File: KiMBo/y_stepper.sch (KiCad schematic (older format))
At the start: 25 parts, among them U25 TMC2130

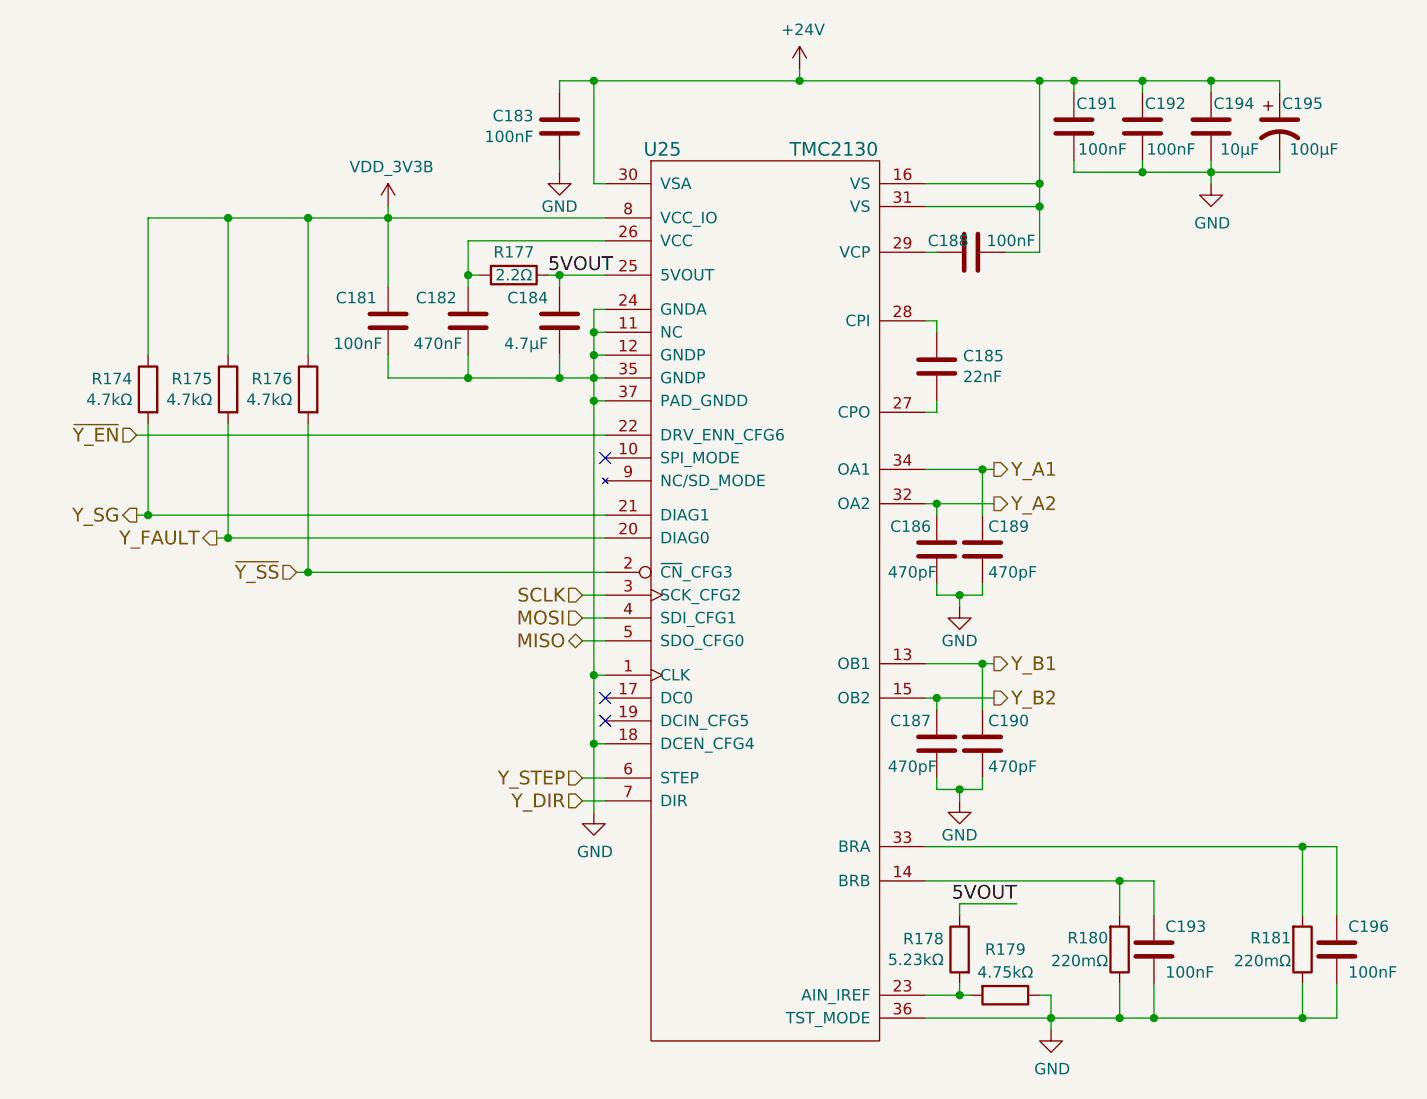
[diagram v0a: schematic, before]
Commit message: Leave SPI0 free for a display, reassign pins so SPI1 is available
Fix some typos/errors
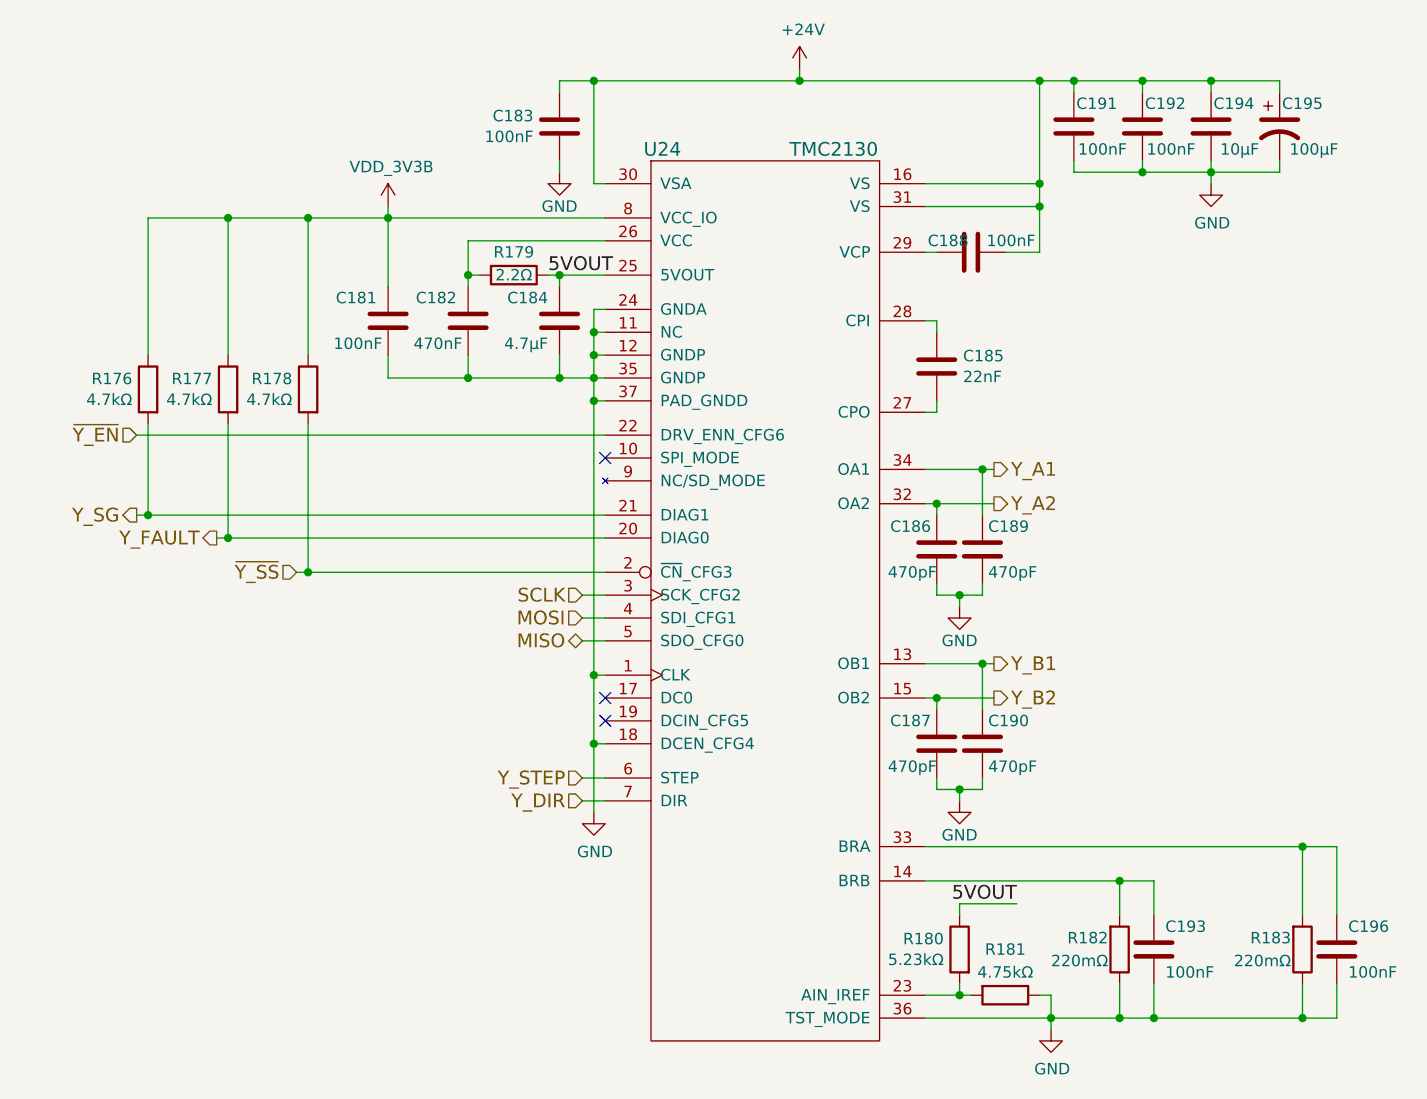
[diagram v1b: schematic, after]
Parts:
- renumbered R174 to R176, R175 to R177, R176 to R178, R177 to R179, R178 to R180, R179 to R181, R180 to R182, R181 to R183, U25 to U24
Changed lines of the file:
@@
 $EndComp
 $Comp
-L GND #PWR0248
+L GND #PWR0247
 U 1 1 58C0B231
 P 6550 3450
-F 0 "#PWR0248" H 6550 3200 50  0001 C CNN
+F 0 "#PWR0247" H 6550 3200 50  0001 C CNN
 F 1 "GND" H 6550 3300 50  0000 C CNN
 F 2 "" H 6550 3450 50  0000 C CNN
@@
 $EndComp
 $Comp
-L GND #PWR0249
+L GND #PWR0248
 U 1 1 58C0B23E
 P 9400 3500
-F 0 "#PWR0249" H 9400 3250 50  0001 C CNN
+F 0 "#PWR0248" H 9400 3250 50  0001 C CNN
 F 1 "GND" H 9405 3327 50  0000 C CNN
 F 2 "" H 9400 3500 50  0000 C CNN
@@
 $EndComp
 $Comp
-L +24V #PWR0250
+L +24V #PWR0249
 U 1 1 58C0B244
 P 7600 3000
-F 0 "#PWR0250" H 7600 2850 50  0001 C CNN
+F 0 "#PWR0249" H 7600 2850 50  0001 C CNN
 F 1 "+24V" H 7615 3173 50  0000 C CNN
 F 2 "" H 7600 3000 50  0000 C CNN
@@
 $EndComp
 $Comp
-L R R181
+L R R183
 U 1 1 58C0B251
 P 9800 6850
-F 0 "R181" H 9750 6800 50  0000 R CNN
+F 0 "R183" H 9750 6800 50  0000 R CNN
 F 1 "220mΩ" H 9750 6900 50  0000 R CNN
 F 2 "" V 9730 6850 50  0001 C CNN
@@
 $EndComp
 $Comp
-L R R180
+L R R182
 U 1 1 58C0B258
 P 9000 6850
-F 0 "R180" H 8950 6800 50  0000 R CNN
+F 0 "R182" H 8950 6800 50  0000 R CNN
 F 1 "220mΩ" H 8950 6900 50  0000 R CNN
 F 2 "" V 8930 6850 50  0001 C CNN
@@
 $EndComp
 $Comp
-L GND #PWR0251
+L GND #PWR0250
 U 1 1 58C0B25F
 P 8700 7200
-F 0 "#PWR0251" H 8700 6950 50  0001 C CNN
+F 0 "#PWR0250" H 8700 6950 50  0001 C CNN
 F 1 "GND" H 8705 7027 50  0000 C CNN
 F 2 "" H 8700 7200 50  0000 C CNN
@@
 NoConn ~ 6750 5750
 $Comp
-L R R177
+L R R179
 U 1 1 58C0B266
 P 6350 3900
-F 0 "R177" V 6250 3900 50  0000 C CNN
+F 0 "R179" V 6250 3900 50  0000 C CNN
 F 1 "2.2Ω" V 6350 3900 50  0000 C CNN
 F 2 "" V 6280 3900 50  0001 C CNN
@@
 NoConn ~ 6750 5850
 $Comp
-L GND #PWR0252
+L GND #PWR0251
 U 1 1 58C0B282
 P 6700 6250
-F 0 "#PWR0252" H 6700 6000 50  0001 C CNN
+F 0 "#PWR0251" H 6700 6000 50  0001 C CNN
 F 1 "GND" H 6705 6077 50  0000 C CNN
 F 2 "" H 6700 6250 50  0000 C CNN
@@
 Y_FAULT
 $Comp
-L R R175
+L R R177
 U 1 1 58C0B290
 P 5100 4400
-F 0 "R175" H 5169 4446 50  0000 L CNN
+F 0 "R177" H 5169 4446 50  0000 L CNN
 F 1 "4.7kΩ" H 5169 4355 50  0000 L CNN
 F 2 "" V 5030 4400 50  0001 C CNN
@@
 5VOUT
 $Comp
-L R R178
+L R R180
 U 1 1 58C0B2A2
 P 8300 6850
-F 0 "R178" H 8369 6896 50  0000 L CNN
+F 0 "R180" H 8369 6896 50  0000 L CNN
 F 1 "5.23kΩ" H 8369 6805 50  0000 L CNN
 F 2 "" V 8230 6850 50  0001 C CNN
@@
 5VOUT
 $Comp
-L R R179
+L R R181
 U 1 1 58C0B2AA
 P 8500 7050
-F 0 "R179" V 8300 7050 50  0000 C CNN
+F 0 "R181" V 8300 7050 50  0000 C CNN
 F 1 "4.75kΩ" V 8400 7050 50  0000 C CNN
 F 2 "" V 8430 7050 50  0001 C CNN
@@
 $EndComp
 $Comp
-L R R176
+L R R178
 U 1 1 58C0B2B1
 P 5450 4400
-F 0 "R176" H 5519 4446 50  0000 L CNN
+F 0 "R178" H 5519 4446 50  0000 L CNN
 F 1 "4.7kΩ" H 5519 4355 50  0000 L CNN
 F 2 "" V 5380 4400 50  0001 C CNN
@@
 $EndComp
 $Comp
-L GND #PWR0253
+L GND #PWR0252
 U 1 1 58C0B2C6
 P 8300 5350
-F 0 "#PWR0253" H 8300 5100 50  0001 C CNN
+F 0 "#PWR0252" H 8300 5100 50  0001 C CNN
 F 1 "GND" H 8300 5200 50  0000 C CNN
 F 2 "" H 8300 5350 50  0000 C CNN
@@
 $EndComp
 $Comp
-L GND #PWR0254
+L GND #PWR0253
 U 1 1 58C0B2DA
 P 8300 6200
-F 0 "#PWR0254" H 8300 5950 50  0001 C CNN
+F 0 "#PWR0253" H 8300 5950 50  0001 C CNN
 F 1 "GND" H 8300 6050 50  0000 C CNN
 F 2 "" H 8300 6200 50  0000 C CNN
@@
 $EndComp
 $Comp
-L TMC2130 U25
+L TMC2130 U24
 U 1 1 58C0B2E7
 P 7450 4850
-F 0 "U25" H 7000 6350 60  0000 C CNN
+F 0 "U24" H 7000 6350 60  0000 C CNN
 F 1 "TMC2130" H 7750 6350 60  0000 C CNN
 F 2 "" H 7450 5150 60  0001 C CNN
@@
 	8200 6150 8200 6100
 $Comp
-L R R174
+L R R176
 U 1 1 58C0B35B
 P 4750 4400
-F 0 "R174" H 4819 4446 50  0000 L CNN
+F 0 "R176" H 4819 4446 50  0000 L CNN
 F 1 "4.7kΩ" H 4819 4355 50  0000 L CNN
 F 2 "" V 4680 4400 50  0001 C CNN
@@
 	4750 3650 6750 3650
 $Comp
-L VDD_3V3B #PWR0255
+L VDD_3V3B #PWR0254
 U 1 1 5A300CA5
 P 5800 3600
-F 0 "#PWR0255" H 5800 3450 50  0001 C CNN
+F 0 "#PWR0254" H 5800 3450 50  0001 C CNN
 F 1 "VDD_3V3B" H 5815 3773 50  0000 C CNN
 F 2 "" H 5800 3600 50  0000 C CNN

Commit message: Use fixed 5V LM2592HV Buck, include SPI0 header for LCD
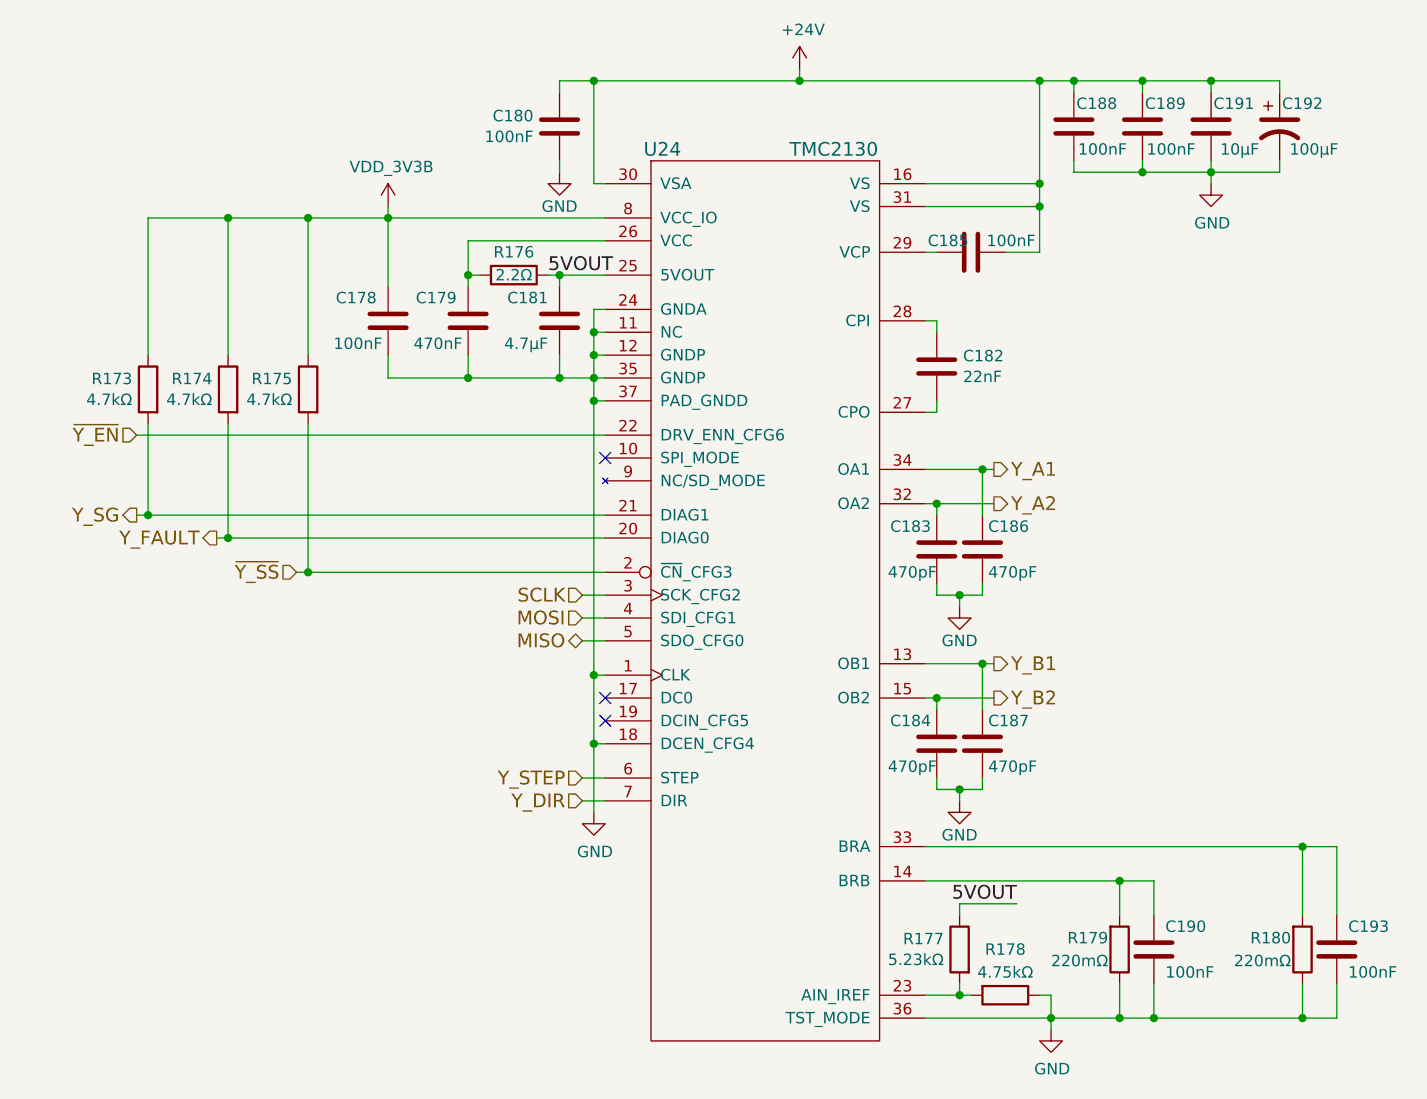
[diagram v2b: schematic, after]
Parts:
- renumbered C181 to C178, C182 to C179, C183 to C180, C184 to C181, C185 to C182, C186 to C183, C187 to C184, C188 to C185, C189 to C186, C190 to C187, C191 to C188, C192 to C189, C193 to C190, C194 to C191, C195 to C192, C196 to C193, R176 to R173, R177 to R174, R178 to R175, R179 to R176, R180 to R177, R181 to R178, R182 to R179, R183 to R180
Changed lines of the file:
@@
 Y_SG
 $Comp
-L C C183
+L C C180
 U 1 1 58C0B215
 P 6550 3250
-F 0 "C183" H 6436 3204 50  0000 R CNN
+F 0 "C180" H 6436 3204 50  0000 R CNN
 F 1 "100nF" H 6436 3295 50  0000 R CNN
 F 2 "Capacitors_SMD:C_0603" H 6588 3100 50  0001 C CNN
@@
 $EndComp
 $Comp
-L C C188
+L C C185
 U 1 1 58C0B21C
 P 8350 3800
-F 0 "C188" V 8300 3700 50  0000 C CNN
+F 0 "C185" V 8300 3700 50  0000 C CNN
 F 1 "100nF" V 8300 3975 50  0000 C CNN
 F 2 "Capacitors_SMD:C_0603" H 8388 3650 50  0001 C CNN
@@
 $EndComp
 $Comp
-L CP1 C195
+L CP1 C192
 U 1 1 58C0B223
 P 9700 3250
-F 0 "C195" H 9800 3350 50  0000 C CNN
+F 0 "C192" H 9800 3350 50  0000 C CNN
 F 1 "100μF" H 9850 3150 50  0000 C CNN
 F 2 "Capacitors_SMD:c_elec_8x10" H 9700 3250 50  0001 C CNN
@@
 $EndComp
 $Comp
-L C C191
+L C C188
 U 1 1 58C0B22A
 P 8800 3250
-F 0 "C191" H 8700 3350 50  0000 C CNN
+F 0 "C188" H 8700 3350 50  0000 C CNN
 F 1 "100nF" H 8675 3150 50  0000 C CNN
 F 2 "Capacitors_SMD:C_0603" H 8838 3100 50  0001 C CNN
@@
 $EndComp
 $Comp
-L GND #PWR0247
+L GND #PWR0242
 U 1 1 58C0B231
 P 6550 3450
-F 0 "#PWR0247" H 6550 3200 50  0001 C CNN
+F 0 "#PWR0242" H 6550 3200 50  0001 C CNN
 F 1 "GND" H 6550 3300 50  0000 C CNN
 F 2 "" H 6550 3450 50  0000 C CNN
@@
 $EndComp
 $Comp
-L C C192
+L C C189
 U 1 1 58C0B237
 P 9100 3250
-F 0 "C192" H 9000 3350 50  0000 C CNN
+F 0 "C189" H 9000 3350 50  0000 C CNN
 F 1 "100nF" H 8975 3150 50  0000 C CNN
 F 2 "Capacitors_SMD:C_0603" H 9138 3100 50  0001 C CNN
@@
 $EndComp
 $Comp
-L GND #PWR0248
+L GND #PWR0243
 U 1 1 58C0B23E
 P 9400 3500
-F 0 "#PWR0248" H 9400 3250 50  0001 C CNN
+F 0 "#PWR0243" H 9400 3250 50  0001 C CNN
 F 1 "GND" H 9405 3327 50  0000 C CNN
 F 2 "" H 9400 3500 50  0000 C CNN
@@
 $EndComp
 $Comp
-L +24V #PWR0249
+L +24V #PWR0244
 U 1 1 58C0B244
 P 7600 3000
-F 0 "#PWR0249" H 7600 2850 50  0001 C CNN
+F 0 "#PWR0244" H 7600 2850 50  0001 C CNN
 F 1 "+24V" H 7615 3173 50  0000 C CNN
 F 2 "" H 7600 3000 50  0000 C CNN
@@
 $EndComp
 $Comp
-L C C185
+L C C182
 U 1 1 58C0B24A
 P 8200 4300
-F 0 "C185" H 8315 4346 50  0000 L CNN
+F 0 "C182" H 8315 4346 50  0000 L CNN
 F 1 "22nF" H 8315 4255 50  0000 L CNN
 F 2 "Capacitors_SMD:C_0402" H 8238 4150 50  0001 C CNN
@@
 $EndComp
 $Comp
-L R R183
+L R R180
 U 1 1 58C0B251
 P 9800 6850
-F 0 "R183" H 9750 6800 50  0000 R CNN
+F 0 "R180" H 9750 6800 50  0000 R CNN
 F 1 "220mΩ" H 9750 6900 50  0000 R CNN
 F 2 "" V 9730 6850 50  0001 C CNN
@@
 $EndComp
 $Comp
-L R R182
+L R R179
 U 1 1 58C0B258
 P 9000 6850
-F 0 "R182" H 8950 6800 50  0000 R CNN
+F 0 "R179" H 8950 6800 50  0000 R CNN
 F 1 "220mΩ" H 8950 6900 50  0000 R CNN
 F 2 "" V 8930 6850 50  0001 C CNN
@@
 $EndComp
 $Comp
-L GND #PWR0250
+L GND #PWR0245
 U 1 1 58C0B25F
 P 8700 7200
-F 0 "#PWR0250" H 8700 6950 50  0001 C CNN
+F 0 "#PWR0245" H 8700 6950 50  0001 C CNN
 F 1 "GND" H 8705 7027 50  0000 C CNN
 F 2 "" H 8700 7200 50  0000 C CNN
@@
 NoConn ~ 6750 5750
 $Comp
-L R R179
+L R R176
 U 1 1 58C0B266
 P 6350 3900
-F 0 "R179" V 6250 3900 50  0000 C CNN
+F 0 "R176" V 6250 3900 50  0000 C CNN
 F 1 "2.2Ω" V 6350 3900 50  0000 C CNN
 F 2 "" V 6280 3900 50  0001 C CNN
@@
 $EndComp
 $Comp
-L C C182
+L C C179
 U 1 1 58C0B26D
 P 6150 4100
-F 0 "C182" H 6200 4200 50  0000 L CNN
+F 0 "C179" H 6200 4200 50  0000 L CNN
 F 1 "470nF" H 6175 4000 50  0000 L CNN
 F 2 "Capacitors_SMD:C_0603" H 6188 3950 50  0001 C CNN
@@
 NoConn ~ 6750 5850
 $Comp
-L GND #PWR0251
+L GND #PWR0246
 U 1 1 58C0B282
 P 6700 6250
-F 0 "#PWR0251" H 6700 6000 50  0001 C CNN
+F 0 "#PWR0246" H 6700 6000 50  0001 C CNN
 F 1 "GND" H 6705 6077 50  0000 C CNN
 F 2 "" H 6700 6250 50  0000 C CNN
@@
 $EndComp
 $Comp
-L C C193
+L C C190
 U 1 1 58C0B288
 P 9150 6850
-F 0 "C193" H 9200 6950 50  0000 L CNN
+F 0 "C190" H 9200 6950 50  0000 L CNN
 F 1 "100nF" H 9200 6750 50  0000 L CNN
 F 2 "Capacitors_SMD:C_0603" H 9188 6700 50  0001 C CNN
@@
 Y_FAULT
 $Comp
-L R R177
+L R R174
 U 1 1 58C0B290
 P 5100 4400
-F 0 "R177" H 5169 4446 50  0000 L CNN
+F 0 "R174" H 5169 4446 50  0000 L CNN
 F 1 "4.7kΩ" H 5169 4355 50  0000 L CNN
 F 2 "" V 5030 4400 50  0001 C CNN
@@
 NoConn ~ 6750 4700
 $Comp
-L C C184
+L C C181
 U 1 1 58C0B29A
 P 6550 4100
-F 0 "C184" H 6600 4200 50  0000 L CNN
+F 0 "C181" H 6600 4200 50  0000 L CNN
 F 1 "4.7μF" H 6600 4000 50  0000 L CNN
 F 2 "Capacitors_SMD:C_0402" H 6588 3950 50  0001 C CNN
@@
 5VOUT
 $Comp
-L R R180
+L R R177
 U 1 1 58C0B2A2
 P 8300 6850
-F 0 "R180" H 8369 6896 50  0000 L CNN
+F 0 "R177" H 8369 6896 50  0000 L CNN
 F 1 "5.23kΩ" H 8369 6805 50  0000 L CNN
 F 2 "" V 8230 6850 50  0001 C CNN
@@
 5VOUT
 $Comp
-L R R181
+L R R178
 U 1 1 58C0B2AA
 P 8500 7050
-F 0 "R181" V 8300 7050 50  0000 C CNN
+F 0 "R178" V 8300 7050 50  0000 C CNN
 F 1 "4.75kΩ" V 8400 7050 50  0000 C CNN
 F 2 "" V 8430 7050 50  0001 C CNN
@@
 $EndComp
 $Comp
-L R R178
+L R R175
 U 1 1 58C0B2B1
 P 5450 4400
-F 0 "R178" H 5519 4446 50  0000 L CNN
+F 0 "R175" H 5519 4446 50  0000 L CNN
 F 1 "4.7kΩ" H 5519 4355 50  0000 L CNN
 F 2 "" V 5380 4400 50  0001 C CNN
@@
 $EndComp
 $Comp
-L C C196
+L C C193
 U 1 1 58C0B2B8
 P 9950 6850
-F 0 "C196" H 10000 6950 50  0000 L CNN
+F 0 "C193" H 10000 6950 50  0000 L CNN
 F 1 "100nF" H 10000 6750 50  0000 L CNN
 F 2 "Capacitors_SMD:C_0603" H 9988 6700 50  0001 C CNN
@@
 $EndComp
 $Comp
-L C C186
+L C C183
 U 1 1 58C0B2BF
 P 8200 5100
-F 0 "C186" H 8225 5200 50  0000 L CNN
+F 0 "C183" H 8225 5200 50  0000 L CNN
 F 1 "470pF" H 8200 5000 50  0000 L CNN
 F 2 "Capacitors_SMD:C_0603" H 8238 4950 50  0001 C CNN
@@
 $EndComp
 $Comp
-L GND #PWR0252
+L GND #PWR0247
 U 1 1 58C0B2C6
 P 8300 5350
-F 0 "#PWR0252" H 8300 5100 50  0001 C CNN
+F 0 "#PWR0247" H 8300 5100 50  0001 C CNN
 F 1 "GND" H 8300 5200 50  0000 C CNN
 F 2 "" H 8300 5350 50  0000 C CNN
@@
 $EndComp
 $Comp
-L C C189
+L C C186
 U 1 1 58C0B2CC
 P 8400 5100
-F 0 "C189" H 8425 5200 50  0000 L CNN
+F 0 "C186" H 8425 5200 50  0000 L CNN
 F 1 "470pF" H 8425 5000 50  0000 L CNN
 F 2 "Capacitors_SMD:C_0603" H 8438 4950 50  0001 C CNN
@@
 $EndComp
 $Comp
-L C C187
+L C C184
 U 1 1 58C0B2D3
 P 8200 5950
-F 0 "C187" H 8225 6050 50  0000 L CNN
+F 0 "C184" H 8225 6050 50  0000 L CNN
 F 1 "470pF" H 8200 5850 50  0000 L CNN
 F 2 "Capacitors_SMD:C_0603" H 8238 5800 50  0001 C CNN
@@
 $EndComp
 $Comp
-L GND #PWR0253
+L GND #PWR0248
 U 1 1 58C0B2DA
 P 8300 6200
-F 0 "#PWR0253" H 8300 5950 50  0001 C CNN
+F 0 "#PWR0248" H 8300 5950 50  0001 C CNN
 F 1 "GND" H 8300 6050 50  0000 C CNN
 F 2 "" H 8300 6200 50  0000 C CNN
@@
 $EndComp
 $Comp
-L C C190
+L C C187
 U 1 1 58C0B2E0
 P 8400 5950
-F 0 "C190" H 8425 6050 50  0000 L CNN
+F 0 "C187" H 8425 6050 50  0000 L CNN
 F 1 "470pF" H 8425 5850 50  0000 L CNN
 F 2 "Capacitors_SMD:C_0603" H 8438 5800 50  0001 C CNN
@@
 	8200 6150 8200 6100
 $Comp
-L R R176
+L R R173
 U 1 1 58C0B35B
 P 4750 4400
-F 0 "R176" H 4819 4446 50  0000 L CNN
+F 0 "R173" H 4819 4446 50  0000 L CNN
 F 1 "4.7kΩ" H 4819 4355 50  0000 L CNN
 F 2 "" V 4680 4400 50  0001 C CNN
@@
 Connection ~ 5100 3650
 $Comp
-L C C194
+L C C191
 U 1 1 58C0B366
 P 9400 3250
-F 0 "C194" H 9300 3350 50  0000 C CNN
+F 0 "C191" H 9300 3350 50  0000 C CNN
 F 1 "10μF" H 9275 3150 50  0000 C CNN
 F 2 "Capacitors_SMD:C_0805" H 9438 3100 50  0001 C CNN
@@
 	4750 3650 6750 3650
 $Comp
-L VDD_3V3B #PWR0254
+L VDD_3V3B #PWR0249
 U 1 1 5A300CA5
 P 5800 3600
-F 0 "#PWR0254" H 5800 3450 50  0001 C CNN
+F 0 "#PWR0249" H 5800 3450 50  0001 C CNN
 F 1 "VDD_3V3B" H 5815 3773 50  0000 C CNN
 F 2 "" H 5800 3600 50  0000 C CNN
@@
 $EndComp
 $Comp
-L C C181
+L C C178
 U 1 1 5A89AE9E
 P 5800 4100
-F 0 "C181" H 5850 4200 50  0000 L CNN
+F 0 "C178" H 5850 4200 50  0000 L CNN
 F 1 "100nF" H 5825 4000 50  0000 L CNN
 F 2 "Capacitors_SMD:C_0603" H 5838 3950 50  0001 C CNN
